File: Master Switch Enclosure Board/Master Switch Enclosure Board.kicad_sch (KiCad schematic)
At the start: 14 parts, among them J1 Harness In A, J2 Harness In B, J3 Harness Out, J4 Screw_Terminal_01x04, J5 Screw_Terminal_01x04, J6 20-pin MicroFit, J7 4-pin MicroFit

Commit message: finished routing
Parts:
- removed J3: Harness Out, Connector_Molex:Molex_Micro-Fit_3.0_43045-2012_2x10_P3.00mm_Vertical, symbol Connector:Conn_01x20_Female
- added J3: Harness Out, Connector_Molex:Molex_Micro-Fit_3.0_43045-2412_2x12_P3.00mm_Vertical, symbol Connector:Conn_01x24_Female
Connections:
- net BSPDTest_in: now also J2.7 (Pin_7); no longer J2.18 (Pin_18)
- net BSPDTest_out: now also J2.6 (Pin_6); no longer J2.19 (Pin_19)
- net BYP_out: now also J1.16 (Pin_16), J5.4 (Pin_4); no longer J1.15 (Pin_15), J4.2 (Pin_2)
- net CANH_EM: now also J2.9 (Pin_9); no longer J1.19 (Pin_19)
- net CANH_Tel: now also J1.18 (Pin_18), J3.21 (Pin_21); no longer J2.1 (Pin_1)
- net CANH_VCU1: now also J2.18 (Pin_18), J6.14 (Pin_14), J3.9 (Pin_9); no longer J2.5 (Pin_5), J6.15 (Pin_15)
- net CANH_VCU2: now also J1.13 (Pin_13), J3.11 (Pin_11); no longer J2.7 (Pin_7)
- net CANH_VCU3: now also J2.5 (Pin_5), J3.13 (Pin_13); no longer J2.9 (Pin_9)
- net CANH_VCU4: now also J2.14 (Pin_14), J3.15 (Pin_15); no longer J2.11 (Pin_11)
- net CANH_ret_Tel: now also J1.15 (Pin_15), J3.23 (Pin_23); no longer J2.3 (Pin_3)
- net CANH_ret_VCU2: now also J2.3 (Pin_3), J3.17 (Pin_17); no longer J2.13 (Pin_13)
- net CANH_ret_VCU3: now also J2.12 (Pin_12), J3.19 (Pin_19); no longer J2.15 (Pin_15)
- net CANL_EM: now also J2.8 (Pin_8); no longer J1.20 (Pin_20)
- net CANL_Tel: now also J1.17 (Pin_17), J3.22 (Pin_22); no longer J2.2 (Pin_2)
- net CANL_VCU1: now also J2.17 (Pin_17), J6.15 (Pin_15), J3.10 (Pin_10); no longer J2.6 (Pin_6), J6.14 (Pin_14)
- net CANL_VCU2: now also J1.12 (Pin_12), J3.12 (Pin_12); no longer J2.8 (Pin_8)
- net CANL_VCU3: now also J2.4 (Pin_4), J3.14 (Pin_14); no longer J2.10 (Pin_10)
- net CANL_VCU4: now also J2.13 (Pin_13), J3.16 (Pin_16); no longer J2.12 (Pin_12)
- net CANL_ret_Tel: now also J1.14 (Pin_14), J3.24 (Pin_24); no longer J2.4 (Pin_4)
- net CANL_ret_VCU2: now also J2.2 (Pin_2), J3.18 (Pin_18); no longer J2.14 (Pin_14)
- net CANL_ret_VCU3: now also J2.11 (Pin_11), J3.20 (Pin_20); no longer J2.16 (Pin_16)
- net CHRG_in: now also J2.10 (Pin_10), J6.11 (Pin_11); no longer J1.16 (Pin_16), J6.9 (Pin_9)
- net GND: now also J2.1 (Pin_1), J3.1 (Pin_1); no longer J2.17 (Pin_17)
- net LVBAT_in: now also J1.10 (Pin_10), J1.6 (Pin_6), J1.7 (Pin_7), J1.8 (Pin_8), J1.9 (Pin_9); no longer J1.1 (Pin_1), J1.2 (Pin_2), J1.3 (Pin_3), J1.4 (Pin_4), J1.5 (Pin_5)
- net LVBAT_sw: now also J4.2 (Pin_2); no longer J5.4 (Pin_4)
- net LV_mastersw_out: now also J1.1 (Pin_1), J1.2 (Pin_2), J1.3 (Pin_3), J1.4 (Pin_4), J1.5 (Pin_5), J3.2 (Pin_2), J3.3 (Pin_3), J3.4 (Pin_4), J3.5 (Pin_5), J3.6 (Pin_6); no longer J1.10 (Pin_10), J1.6 (Pin_6), J1.7 (Pin_7), J1.8 (Pin_8), J1.9 (Pin_9)
- net RST_out: now also J2.15 (Pin_15), J6.10 (Pin_10); no longer J1.14 (Pin_14), J6.8 (Pin_8)
- net SEPIC_out: now also J6.8 (Pin_8), J6.9 (Pin_9); no longer J6.10 (Pin_10), J6.7 (Pin_7)
- net SHDN2_in: now also J2.19 (Pin_19); no longer J1.12 (Pin_12)
- net SHDN2_out: now also J2.20 (Pin_20); no longer J1.13 (Pin_13)
- net TSALEnergized_pt: now also J1.19 (Pin_19), J3.8 (Pin_8); no longer J1.18 (Pin_18)
- net TSALSafe_pt: now also J1.20 (Pin_20), J3.7 (Pin_7); no longer J1.17 (Pin_17)
- net VCUWake_out: now also J2.16 (Pin_16), J6.7 (Pin_7); no longer J2.20 (Pin_20), J6.11 (Pin_11)
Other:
- note added: "11: Charge Detect"
- note added: "7-8: VCU Wake Switch"
- note added: "9-10: Error Reset Button"
- note removed: "1-3: DPDT Switch"
- note removed: "10-11: VCU Wake Switch"
- note removed: "5-6: Master Switch"
- note removed: "7-8: Error Reset Button"
- note removed: "9: Charge Detect"
- moved on the sheet: J2

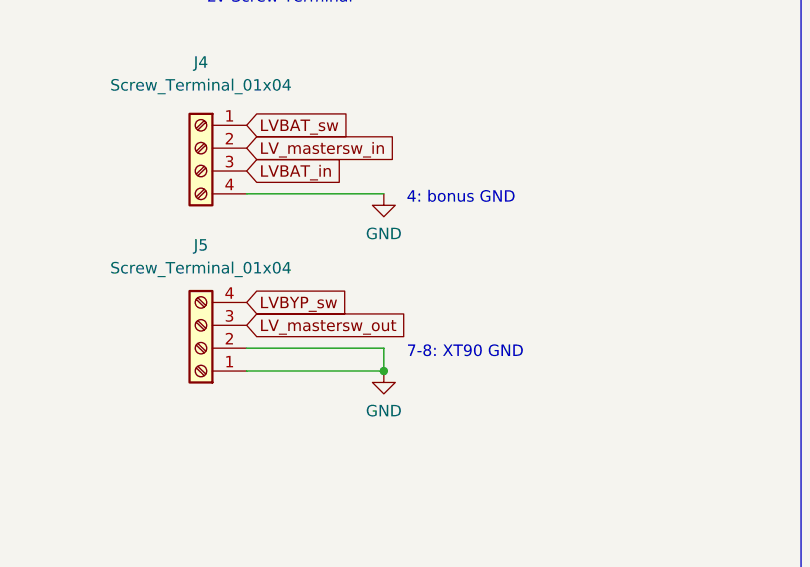
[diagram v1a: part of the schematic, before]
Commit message: less resistance, more spacing
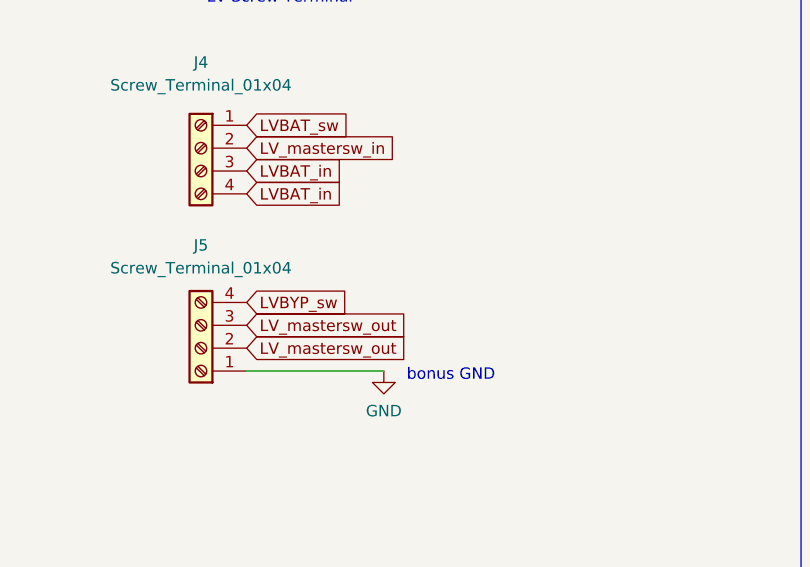
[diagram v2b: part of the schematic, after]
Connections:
- net GND: no longer J4.4 (Pin_4), J5.2 (Pin_2)
- net LVBAT_in: now also J4.4 (Pin_4)
- net LV_mastersw_out: now also J5.2 (Pin_2)
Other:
- note added: "bonus GND"
- note removed: "4: bonus GND"
- note removed: "7-8: XT90 GND"
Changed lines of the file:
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@@
   (junction (at 198.755 62.865) (diameter 0) (color 0 0 0 0)
   )
-  (junction (at 180.975 144.78) (diameter 0) (color 0 0 0 0)
-  )
   (junction (at 46.355 226.06) (diameter 0) (color 0 0 0 0)
   )
@@
     (stroke (width 0) (type default) (color 0 0 0 0))
   )
-  (wire (pts (xy 180.975 125.095) (xy 165.735 125.095))
-    (stroke (width 0) (type default) (color 0 0 0 0))
-  )
   (wire (pts (xy 88.9 81.915) (xy 85.725 81.915))
     (stroke (width 0) (type default) (color 0 0 0 0))
@@
     (stroke (width 0) (type default) (color 0 0 0 0))
   )
-  (wire (pts (xy 180.975 142.24) (xy 180.975 144.78))
-    (stroke (width 0) (type default) (color 0 0 0 0))
-  )
   (wire (pts (xy 42.545 97.155) (xy 39.37 97.155))
     (stroke (width 0) (type default) (color 0 0 0 0))
@@
     (stroke (width 0) (type default) (color 0 0 0 0))
   )
-  (wire (pts (xy 165.735 142.24) (xy 180.975 142.24))
-    (stroke (width 0) (type default) (color 0 0 0 0))
-  )
   (wire (pts (xy 42.545 213.36) (xy 40.005 213.36))
     (stroke (width 0) (type default) (color 0 0 0 0))
@@
     (effects (font (size 1.27 1.27)) (justify left bottom))
   )
-  (text "4: bonus GND" (at 183.515 126.365 0)
-    (effects (font (size 1.27 1.27)) (justify left bottom))
-  )
   (text "18-20: bonus GND" (at 59.055 226.695 0)
     (effects (font (size 1.27 1.27)) (justify left bottom))
@@
     (effects (font (size 1.27 1.27)) (justify left bottom))
   )
-  (text "7-8: XT90 GND" (at 183.515 143.51 0)
+  (text "bonus GND" (at 183.515 146.05 0)
     (effects (font (size 1.27 1.27)) (justify left bottom))
   )
@@
     )
   )
+  (global_label "LV_mastersw_out" (shape input) (at 165.735 142.24 0) (fields_autoplaced)
+    (effects (font (size 1.27 1.27)) (justify left))
+    (property "Intersheet References" "${INTERSHEET_REFS}" (id 0) (at 184.0533 142.3194 0)
+      (effects (font (size 1.27 1.27)) (justify left) hide)
+    )
+  )
   (global_label "SHDN2_in" (shape input) (at 42.545 158.115 0) (fields_autoplaced)
     (effects (font (size 1.27 1.27)) (justify left))
@@
     (effects (font (size 1.27 1.27)) (justify left))
     (property "Intersheet References" "${INTERSHEET_REFS}" (id 0) (at 55.5414 142.7956 0)
+      (effects (font (size 1.27 1.27)) (justify left) hide)
+    )
+  )
+  (global_label "LVBAT_in" (shape input) (at 165.735 125.095 0) (fields_autoplaced)
+    (effects (font (size 1.27 1.27)) (justify left))
+    (property "Intersheet References" "${INTERSHEET_REFS}" (id 0) (at 176.3124 125.0156 0)
       (effects (font (size 1.27 1.27)) (justify left) hide)
     )
@@
     (pin "4")
   )
-  (symbol (lib_id "power:GND") (at 180.975 125.095 0) (unit 1)
-    (in_bom yes) (on_board yes) (fields_autoplaced)
-    (property "Reference" "#PWR01" (id 0) (at 180.975 131.445 0)
-      (effects (font (size 1.27 1.27)) hide)
-    )
-    (property "Value" "GND" (id 1) (at 180.975 129.54 0))
-    (property "Footprint" "" (id 2) (at 180.975 125.095 0)
-      (effects (font (size 1.27 1.27)) hide)
-    )
-    (property "Datasheet" "" (id 3) (at 180.975 125.095 0)
-      (effects (font (size 1.27 1.27)) hide)
-    )
-    (pin "1")
-  )
   (symbol (lib_id "power:GND") (at 168.275 78.105 0) (unit 1)
     (in_bom yes) (on_board yes) (fields_autoplaced)
@@
       (reference "#FLG01") (unit 1) (value "PWR_FLAG") (footprint "")
     )
-    (path "/3bfb8114-bb27-425d-b396-8536c4b85741"
-      (reference "#PWR01") (unit 1) (value "GND") (footprint "")
-    )
     (path "/937320c7-b28a-4852-b286-19284e905545"
